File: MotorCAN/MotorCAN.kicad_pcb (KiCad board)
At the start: 2 copper layers, 60 x 60 mm, 48 parts, among them CN1 ZX-SH1.0-3PWT, CN2 HCZZ0021-4, CN3 HCZZ0021-4, J1 MTR, U1 STM32G431CBT6, U2 DRV8316CRRGFR, U3 TCAN330GDCNR, U4 MT6816CT-AKD-R, X1 XL7EL89CKI-111YLC-24M

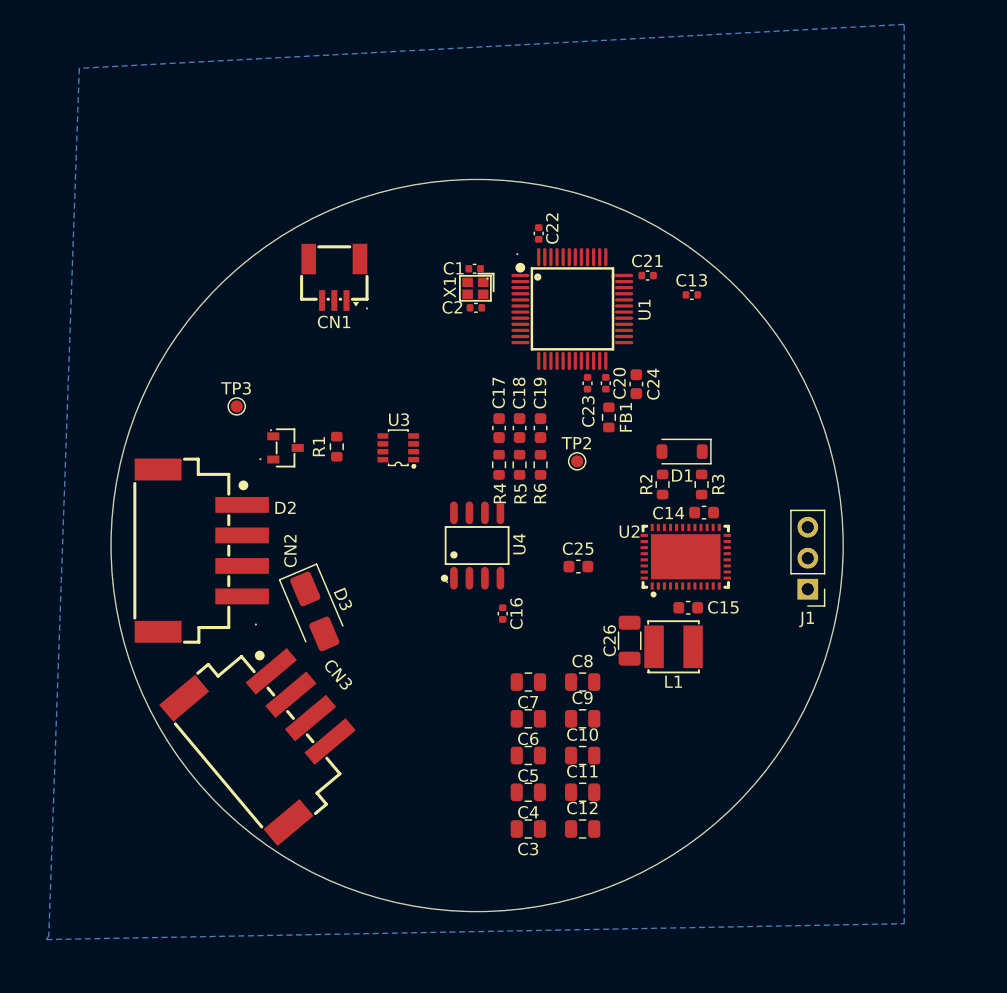
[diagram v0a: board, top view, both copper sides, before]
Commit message: Added finalized design, with some issues fixed
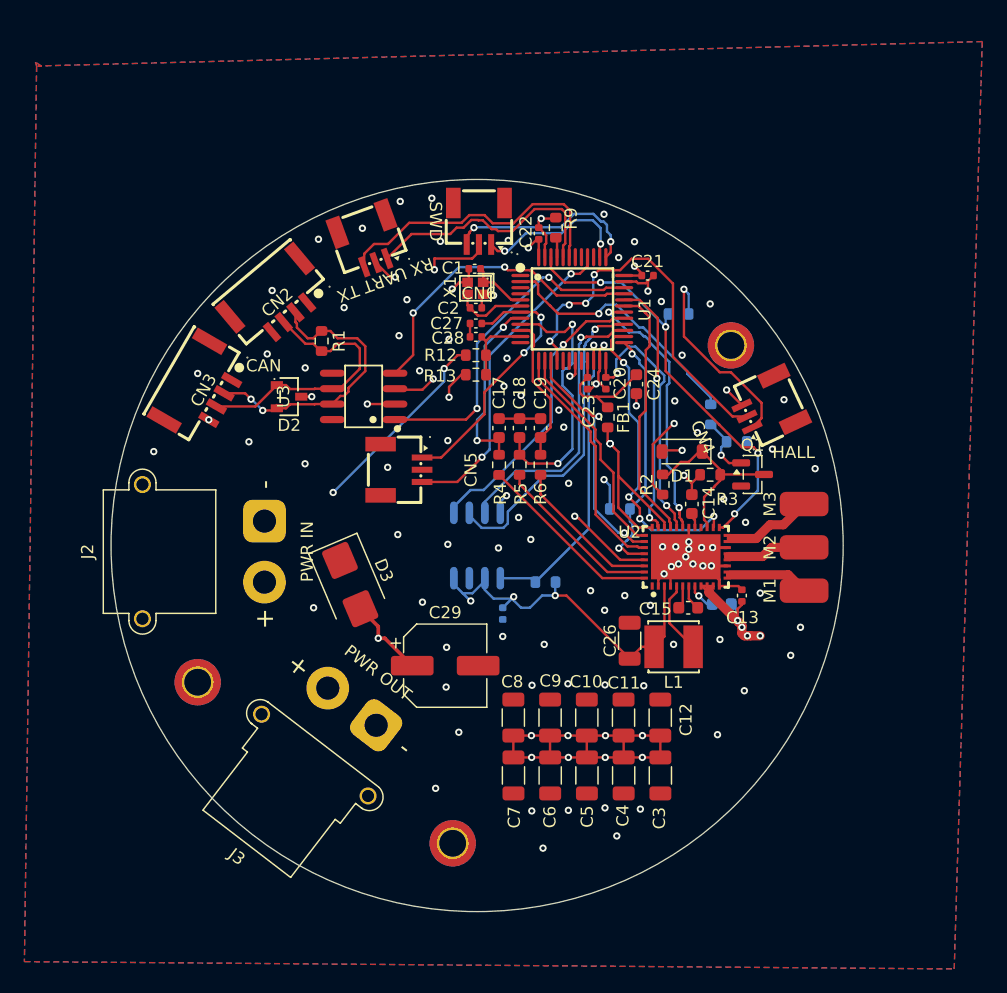
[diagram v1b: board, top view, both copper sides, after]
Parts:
- removed J1: MTR, Connector_PinHeader_2.54mm:PinHeader_1x03_P2.54mm_Vertical
- removed TP2: 3V3, TestPoint:TestPoint_Pad_D1.0mm
- removed TP3: VIN, TestPoint:TestPoint_Pad_D1.0mm
- added C27: 100nF, Capacitor_SMD:C_0402_1005Metric, F.Cu at (119.9, 46.8)
- added C28: 100nF, Capacitor_SMD:C_0402_1005Metric, F.Cu at (119.9, 47.9)
- added C29: 100uF, Capacitor_SMD:CP_Elec_6.3x7.7, F.Cu at (117.4, 74.8)
- added CN4: ZX-SH1.0-3PWT, easyeda2kicad:CONN-SMD_3P-P1.00_MEGASTAR_ZX-SH1.0-3PWT, F.Cu at (143.7, 53.7)
- added CN5: ZX-SH1.0-3PWT, easyeda2kicad:CONN-SMD_3P-P1.00_MEGASTAR_ZX-SH1.0-3PWT, F.Cu at (113.8, 58.8)
- added CN6: ZX-SH1.0-3PWT, easyeda2kicad:CONN-SMD_3P-P1.00_MEGASTAR_ZX-SH1.0-3PWT, F.Cu at (120.2, 38.6)
- added H1: MountingHole_Pad, MountingHole:MountingHole_2.2mm_M2_ISO14580_Pad_TopBottom, F.Cu at (118.0, 89.4)
- added H3: MountingHole_Pad, MountingHole:MountingHole_2.2mm_M2_ISO14580_Pad_TopBottom, F.Cu at (140.8, 48.6)
- added H4: MountingHole_Pad, MountingHole:MountingHole_2.2mm_M2_ISO14580_Pad_TopBottom, F.Cu at (97.1, 76.2)
- added J2: PWR IN, Connector_AMASS:AMASS_XT30PW-M_1x02_P2.50mm_Horizontal, F.Cu at (102.6, 63.0)
- added J3: PWR OUT, Connector_AMASS:AMASS_XT30PW-F_1x02_P2.50mm_Horizontal, F.Cu at (111.7, 79.7)
- added M1: A, Connector_Wire:SolderWirePad_1x01_SMD_2x4mm, F.Cu at (146.8, 68.7)
- added M2: B, Connector_Wire:SolderWirePad_1x01_SMD_2x4mm, F.Cu at (146.8, 65.2)
- added M3: C, Connector_Wire:SolderWirePad_1x01_SMD_2x4mm, F.Cu at (146.8, 61.6)
- added Q1: 2N7002, Package_TO_SOT_SMD:SOT-23, F.Cu at (142.6, 59.2)
- added R10: 10k, Resistor_SMD:R_0603_1608Metric, B.Cu at (131.7, 62.0)
- added R11: 10k, Resistor_SMD:R_0603_1608Metric, B.Cu at (125.6, 68.0)
- added R12: 100k, Resistor_SMD:R_0603_1608Metric, F.Cu at (119.9, 49.4)
- added R13: 10k, Resistor_SMD:R_0603_1608Metric, F.Cu at (119.9, 51.0)
- added R14: 10k, Resistor_SMD:R_0603_1608Metric, B.Cu at (136.5, 46.0)
- added R7: 100k, Resistor_SMD:R_0603_1608Metric, B.Cu at (141.3, 56.5)
- added R8: 100, Resistor_SMD:R_0603_1608Metric, B.Cu at (139.2, 54.2)
- added R9: 10k, Resistor_SMD:R_0603_1608Metric, F.Cu at (126.5, 39.0)
- C10, C11, C12, C3, C4, C5, C6, C7, C8, C9: footprint Capacitor_SMD:C_0805_2012Metric -> Capacitor_SMD:C_1206_3216Metric
- C16, C25, U4: moved to B.Cu
- CN2, CN3: value HCZZ0021-4 -> WAFER-GH1.25-4PWB; footprint easyeda2kicad:CONN-SMD_HCZZ0021-4 -> easyeda2kicad:CONN-SMD_4P-P1.25_XUNPU_WAFER-GH1.25-4PWB
- D3: value 18V -> 26V; footprint Diode_SMD:D_SMA -> Diode_SMD:D_SMB
- U3: value TCAN330GDCNR -> SN65HVD230DR; footprint easyeda2kicad:SOT-23-8_L2.9-W1.6-P0.65-LS2.8-BL -> easyeda2kicad:SOIC-8_L4.9-W3.9-P1.27-LS6.0-BL
- moved CN3 28.6 mm to (97.6, 52.3), turned to -120 degrees
- moved C13 25.0 mm to (141.7, 69.1), turned to -90 degrees
- moved CN2 21.3 mm to (103.6, 45.1), turned to -140 degrees
- moved C25 12.1 mm to (140.1, 69.8)
- moved C3 11.7 mm to (135.0, 83.8), turned to -90 degrees
- moved C12 11.1 mm to (135.0, 79.1), turned to 90 degrees
- moved R1 8.75 mm to (107.3, 48.2), turned to -90 degrees
- moved C4 7.93 mm to (132.0, 83.8), turned to -90 degrees
- moved C7 7.75 mm to (123.0, 83.8), turned to -90 degrees
- moved C11 6.98 mm to (132.0, 79.1), turned to 90 degrees
- moved C8 6.38 mm to (123.0, 79.1), turned to 90 degrees
- moved U3 5.08 mm to (110.7, 52.8)
- moved C5 5.07 mm to (129.0, 83.8), turned to -90 degrees
- moved C6 4.97 mm to (126.0, 83.8), turned to -90 degrees
- moved D2 4.21 mm to (104.6, 52.8)
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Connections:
- net /CANH renamed /CAN+
- net /CANL renamed /CAN-
- C16 pad 1: /3V3 -> +3V3
- CN1 pad 1: /SWDIO -> /UART1RX
- CN1 pad 3: /SWDCLK -> /UART1TX
- CN2 pad 1: /VIN -> unconnected-(CN2-Pad1)
- CN3 pad 1: /VIN -> unconnected-(CN3-Pad1)
- U1 pad 11: /nSCS -> /VREAD
- U1 pad 12: unconnected-(U1-PA4-Pad12) -> /DEBUG
- U1 pad 16: unconnected-(U1-PB0-Pad16) -> /HALL
- U1 pad 2: unconnected-(U1-PC13-Pad2) -> Net-(U1-PC13)
- U1 pad 22: unconnected-(U1-PB10-Pad22) -> /CSENC
- U1 pad 25: unconnected-(U1-PB11-Pad25) -> /nSCS
- U1 pad 27: /INAL -> /SPICLK2
- U1 pad 28: /INBL -> /MISO2
- U1 pad 29: /INCL -> /MOSI2
- U1 pad 40: /SPICLK2 -> /SWO
- U1 pad 41: /MISO2 -> unconnected-(U1-PB4-Pad41)
- U1 pad 42: /MOSI2 -> unconnected-(U1-PB5-Pad42)
- U1 pad 43: /CSENC -> /UART1TX
- U1 pad 44: unconnected-(U1-PB7-Pad44) -> /UART1RX
- U1 pad 45: unconnected-(U1-PB8-BOOT0-Pad45) -> Net-(U1-PB8-BOOT0)
- U1 pad 7: unconnected-(U1-PG10-NRST-Pad7) -> /NRST
- U2 pad 12: Net-(U2-PGND-Pad12) -> GND
- U2 pad 15: Net-(U2-PGND-Pad12) -> GND
- U2 pad 18: Net-(U2-PGND-Pad12) -> GND
- U2 pad 28: /INAL -> +3V3
- U2 pad 30: /INBL -> +3V3
- U2 pad 32: /INCL -> +3V3
- U2 pad 37: unconnected-(U2-VREF/ILIM-Pad37) -> +3V3
- U3 pad 8: unconnected-(U3-S-Pad8) -> GND
- U4 pad 2: /3V3 -> +3V3
- U4 pad 4: /3V3 -> +3V3
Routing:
- net +3V3: track 0.00 -> 105.0 mm, vias 0 -> 13
- net /VIN: track 0.00 -> 75.8 mm, vias 0 -> 16
- net GND: track 0.00 -> 70.2 mm, vias 0 -> 104
- net /DRVOFF: track 0.00 -> 35.1 mm, vias 0 -> 4
- net /HALL: track 0.00 -> 31.8 mm, vias 0 -> 4
- net /TXD: track 0.00 -> 27.2 mm, vias 0 -> 2
- net /MISO2: track 0.00 -> 26.3 mm, vias 0 -> 1
- net /SWO: track 0.00 -> 26.1 mm, vias 0 -> 2
- net /CSENC: track 0.00 -> 25.7 mm, vias 0 -> 1
- net /RXD: track 0.00 -> 25.4 mm, vias 0 -> 2
- net /nFAULT: track 0.00 -> 25.3 mm, vias 0 -> 4
- net /MOSI2: track 0.00 -> 24.3 mm, vias 0 -> 1
- net /UART1TX: track 0.00 -> 24.3 mm
- net /CAN+: track 0.00 -> 24.1 mm, vias 0 -> 2
- net /SPICLK2: track 0.00 -> 23.6 mm, vias 0 -> 1
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- added copper zone on In2.Cu, net +3V3
- added copper zone on In2.Cu, net /VIN
- added copper zone on F.Cu, net GND
- added copper zone on In1.Cu, net GND
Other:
- copper layers 2 -> 4
- board text added: "CAN"
- board text added: "HALL"
- board text added: "RX UART TX"
- board text added: "SWD"
